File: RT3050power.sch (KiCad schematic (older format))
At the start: 30 parts, among them J1 USB, U1 RT3050, U4 LM1117, U5 LM1117

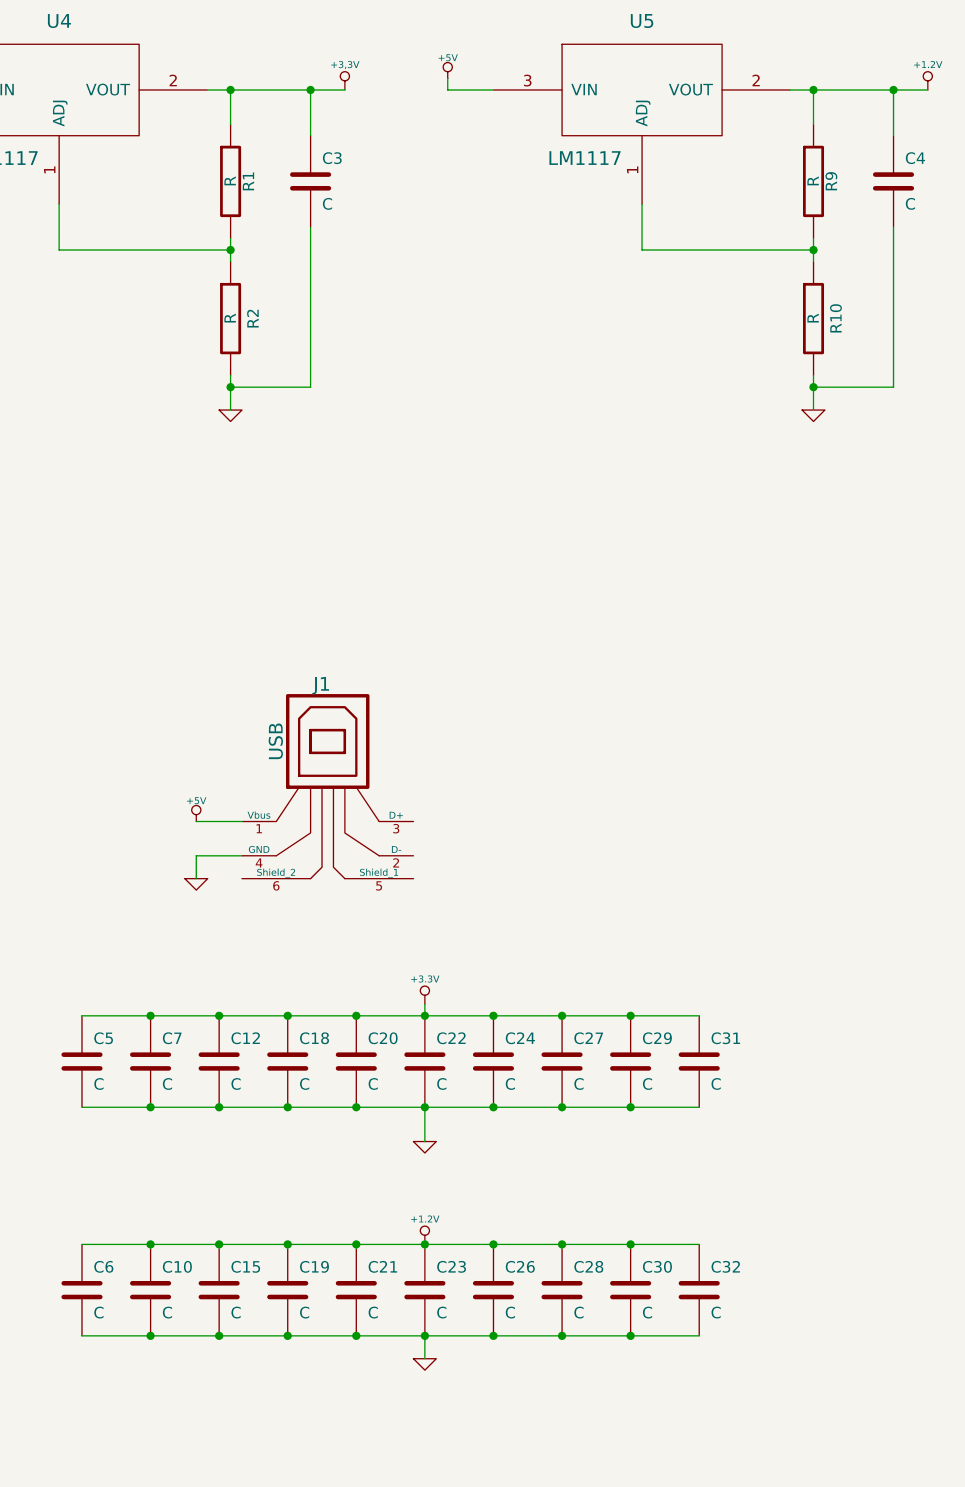
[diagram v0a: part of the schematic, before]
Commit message: updated component values
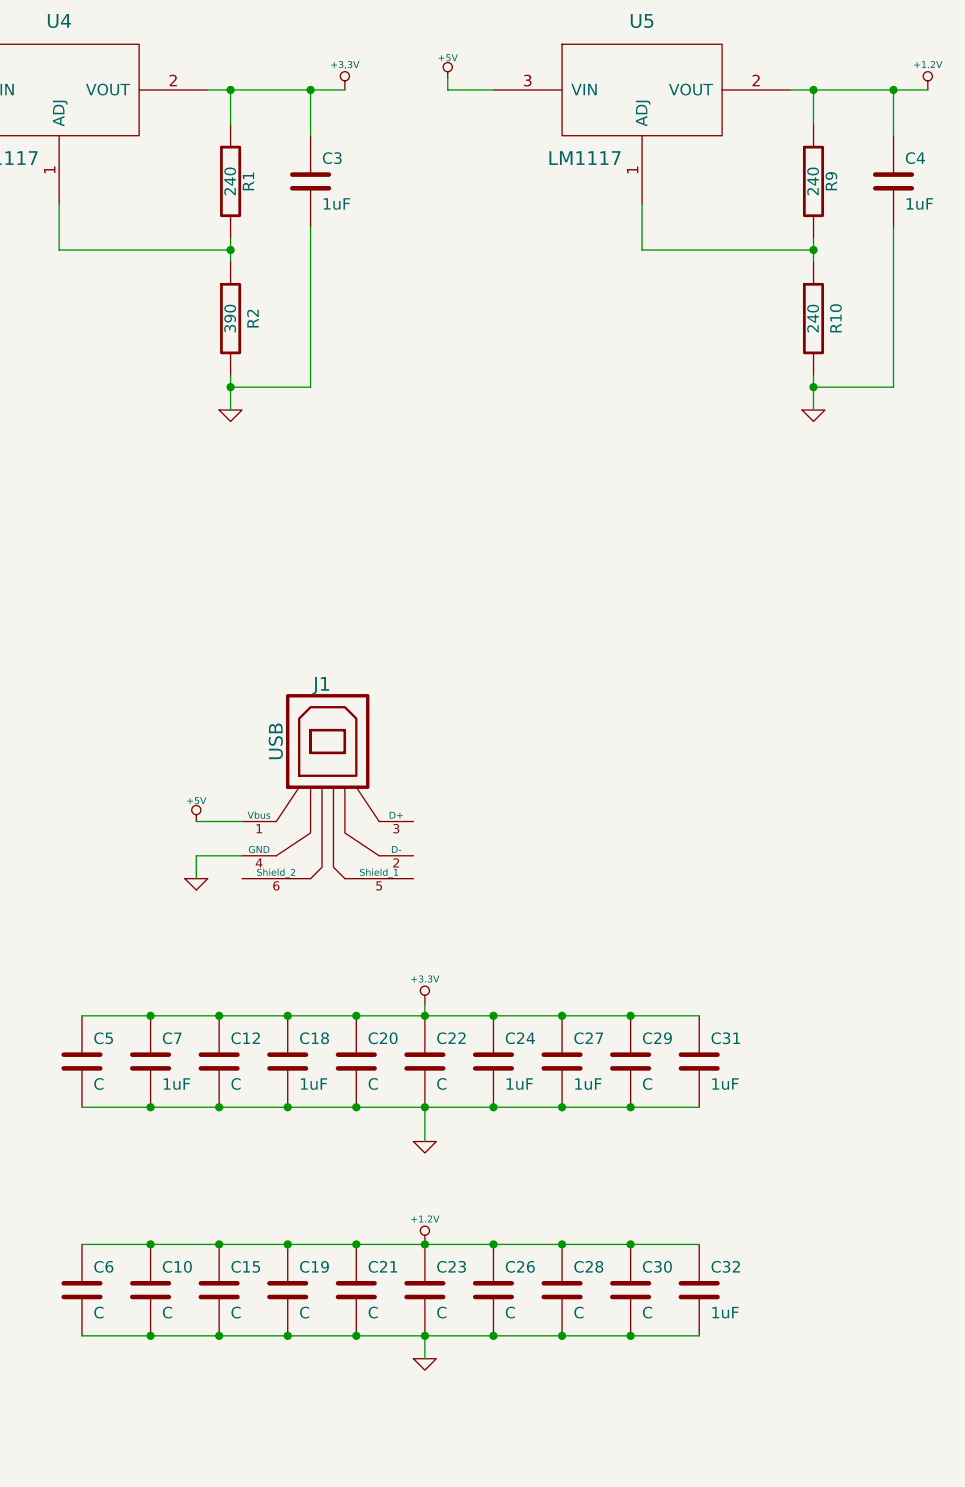
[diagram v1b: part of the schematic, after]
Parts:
- C18, C24, C27, C3, C31, C32, C4, C7: value C -> 1uF
- R1, R10, R9: value R -> 240
- R2: value R -> 390
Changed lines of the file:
@@
-EESchema Schematic File Version 2  date Tue 02 Sep 2014 05:26:51 BST
+EESchema Schematic File Version 2
 LIBS:power
 LIBS:device
@@
 LIBS:AIC809
 LIBS:rt3050-cache
-EELAYER 25  0
+EELAYER 25 0
 EELAYER END
-$Descr A4 11700 8267
+$Descr A4 11693 8268
 encoding utf-8
 Sheet 5 6
@@
 P 9750 6300
 F 0 "C32" H 9800 6400 50  0000 L CNN
-F 1 "C" H 9800 6200 50  0000 L CNN
+F 1 "1uF" H 9800 6200 50  0000 L CNN
+F 2 "" H 9750 6300 60  0001 C CNN
+F 3 "" H 9750 6300 60  0001 C CNN
 	1    9750 6300
 	1    0    0    -1
@@
 F 0 "C30" H 9500 6400 50  0000 L CNN
 F 1 "C" H 9500 6200 50  0000 L CNN
+F 2 "" H 9450 6300 60  0001 C CNN
+F 3 "" H 9450 6300 60  0001 C CNN
 	1    9450 6300
 	1    0    0    -1
@@
 F 0 "C28" H 9200 6400 50  0000 L CNN
 F 1 "C" H 9200 6200 50  0000 L CNN
+F 2 "" H 9150 6300 60  0001 C CNN
+F 3 "" H 9150 6300 60  0001 C CNN
 	1    9150 6300
 	1    0    0    -1
@@
 F 0 "C26" H 8900 6400 50  0000 L CNN
 F 1 "C" H 8900 6200 50  0000 L CNN
+F 2 "" H 8850 6300 60  0001 C CNN
+F 3 "" H 8850 6300 60  0001 C CNN
 	1    8850 6300
 	1    0    0    -1
@@
 F 0 "C23" H 8600 6400 50  0000 L CNN
 F 1 "C" H 8600 6200 50  0000 L CNN
+F 2 "" H 8550 6300 60  0001 C CNN
+F 3 "" H 8550 6300 60  0001 C CNN
 	1    8550 6300
 	1    0    0    -1
@@
 F 0 "C21" H 8300 6400 50  0000 L CNN
 F 1 "C" H 8300 6200 50  0000 L CNN
+F 2 "" H 8250 6300 60  0001 C CNN
+F 3 "" H 8250 6300 60  0001 C CNN
 	1    8250 6300
 	1    0    0    -1
@@
 F 0 "C19" H 8000 6400 50  0000 L CNN
 F 1 "C" H 8000 6200 50  0000 L CNN
+F 2 "" H 7950 6300 60  0001 C CNN
+F 3 "" H 7950 6300 60  0001 C CNN
 	1    7950 6300
 	1    0    0    -1
@@
 F 0 "C15" H 7700 6400 50  0000 L CNN
 F 1 "C" H 7700 6200 50  0000 L CNN
+F 2 "" H 7650 6300 60  0001 C CNN
+F 3 "" H 7650 6300 60  0001 C CNN
 	1    7650 6300
 	1    0    0    -1
@@
 F 0 "C10" H 7400 6400 50  0000 L CNN
 F 1 "C" H 7400 6200 50  0000 L CNN
+F 2 "" H 7350 6300 60  0001 C CNN
+F 3 "" H 7350 6300 60  0001 C CNN
 	1    7350 6300
 	1    0    0    -1
@@
 F 0 "C6" H 7100 6400 50  0000 L CNN
 F 1 "C" H 7100 6200 50  0000 L CNN
+F 2 "" H 7050 6300 60  0001 C CNN
+F 3 "" H 7050 6300 60  0001 C CNN
 	1    7050 6300
 	1    0    0    -1
@@
 P 9750 5300
 F 0 "C31" H 9800 5400 50  0000 L CNN
-F 1 "C" H 9800 5200 50  0000 L CNN
+F 1 "1uF" H 9800 5200 50  0000 L CNN
+F 2 "" H 9750 5300 60  0001 C CNN
+F 3 "" H 9750 5300 60  0001 C CNN
 	1    9750 5300
 	1    0    0    -1
@@
 F 0 "C29" H 9500 5400 50  0000 L CNN
 F 1 "C" H 9500 5200 50  0000 L CNN
+F 2 "" H 9450 5300 60  0001 C CNN
+F 3 "" H 9450 5300 60  0001 C CNN
 	1    9450 5300
 	1    0    0    -1
@@
 P 9150 5300
 F 0 "C27" H 9200 5400 50  0000 L CNN
-F 1 "C" H 9200 5200 50  0000 L CNN
+F 1 "1uF" H 9200 5200 50  0000 L CNN
+F 2 "" H 9150 5300 60  0001 C CNN
+F 3 "" H 9150 5300 60  0001 C CNN
 	1    9150 5300
 	1    0    0    -1
@@
 P 8850 5300
 F 0 "C24" H 8900 5400 50  0000 L CNN
-F 1 "C" H 8900 5200 50  0000 L CNN
+F 1 "1uF" H 8900 5200 50  0000 L CNN
+F 2 "" H 8850 5300 60  0001 C CNN
+F 3 "" H 8850 5300 60  0001 C CNN
 	1    8850 5300
 	1    0    0    -1
@@
 F 0 "C22" H 8600 5400 50  0000 L CNN
 F 1 "C" H 8600 5200 50  0000 L CNN
+F 2 "" H 8550 5300 60  0001 C CNN
+F 3 "" H 8550 5300 60  0001 C CNN
 	1    8550 5300
 	1    0    0    -1
@@
 F 0 "C20" H 8300 5400 50  0000 L CNN
 F 1 "C" H 8300 5200 50  0000 L CNN
+F 2 "" H 8250 5300 60  0001 C CNN
+F 3 "" H 8250 5300 60  0001 C CNN
 	1    8250 5300
 	1    0    0    -1
@@
 P 7950 5300
 F 0 "C18" H 8000 5400 50  0000 L CNN
-F 1 "C" H 8000 5200 50  0000 L CNN
+F 1 "1uF" H 8000 5200 50  0000 L CNN
+F 2 "" H 7950 5300 60  0001 C CNN
+F 3 "" H 7950 5300 60  0001 C CNN
 	1    7950 5300
 	1    0    0    -1
@@
 F 0 "C12" H 7700 5400 50  0000 L CNN
 F 1 "C" H 7700 5200 50  0000 L CNN
+F 2 "" H 7650 5300 60  0001 C CNN
+F 3 "" H 7650 5300 60  0001 C CNN
 	1    7650 5300
 	1    0    0    -1
@@
 P 7350 5300
 F 0 "C7" H 7400 5400 50  0000 L CNN
-F 1 "C" H 7400 5200 50  0000 L CNN
+F 1 "1uF" H 7400 5200 50  0000 L CNN
+F 2 "" H 7350 5300 60  0001 C CNN
+F 3 "" H 7350 5300 60  0001 C CNN
 	1    7350 5300
 	1    0    0    -1
@@
 F 0 "C5" H 7100 5400 50  0000 L CNN
 F 1 "C" H 7100 5200 50  0000 L CNN
+F 2 "" H 7050 5300 60  0001 C CNN
+F 3 "" H 7050 5300 60  0001 C CNN
 	1    7050 5300
 	1    0    0    -1
@@
 F 0 "#PWR027" H 8550 6600 30  0001 C CNN
 F 1 "GND" H 8550 6530 30  0001 C CNN
+F 2 "" H 8550 6600 60  0001 C CNN
+F 3 "" H 8550 6600 60  0001 C CNN
 	1    8550 6600
 	1    0    0    -1
@@
 F 0 "#PWR028" H 8550 6240 20  0001 C CNN
 F 1 "+1.2V" H 8550 6210 30  0000 C CNN
+F 2 "" H 8550 6100 60  0001 C CNN
+F 3 "" H 8550 6100 60  0001 C CNN
 	1    8550 6100
 	1    0    0    -1
@@
 F 0 "#PWR029" H 8550 5650 30  0001 C CNN
 F 1 "GND" H 8550 5580 30  0001 C CNN
+F 2 "" H 8550 5650 60  0001 C CNN
+F 3 "" H 8550 5650 60  0001 C CNN
 	1    8550 5650
 	1    0    0    -1
@@
 F 0 "#PWR030" H 8550 5010 30  0001 C CNN
 F 1 "+3.3V" H 8550 5160 30  0000 C CNN
+F 2 "" H 8550 5050 60  0001 C CNN
+F 3 "" H 8550 5050 60  0001 C CNN
 	1    8550 5050
 	1    0    0    -1
@@
 F 0 "#PWR031" H 5300 4290 20  0001 C CNN
 F 1 "+1.2V" H 5300 4260 30  0000 C CNN
+F 2 "" H 5300 4150 60  0001 C CNN
+F 3 "" H 5300 4150 60  0001 C CNN
 	1    5300 4150
 	1    0    0    -1
@@
 F 0 "#PWR032" H 5150 1090 20  0001 C CNN
 F 1 "+1.2V" H 5150 1060 30  0000 C CNN
+F 2 "" H 5150 950 60  0001 C CNN
+F 3 "" H 5150 950 60  0001 C CNN
 	1    5150 950
 	1    0    0    -1
@@
 F 0 "#PWR033" H 10750 1190 20  0001 C CNN
 F 1 "+1.2V" H 10750 1160 30  0000 C CNN
+F 2 "" H 10750 1050 60  0001 C CNN
+F 3 "" H 10750 1050 60  0001 C CNN
 	1    10750 1050
 	1    0    0    -1
@@
 F 0 "U4" H 6950 2050 60  0000 C CNN
 F 1 "LM1117" H 6700 1450 60  0000 C CNN
+F 2 "" H 6950 1400 60  0001 C CNN
+F 3 "" H 6950 1400 60  0001 C CNN
 	1    6950 1400
 	1    0    0    -1
@@
 F 0 "#PWR034" H 5100 8410 30  0001 C CNN
 F 1 "+3,3V" H 5100 8560 30  0000 C CNN
+F 2 "" H 5100 8450 60  0001 C CNN
+F 3 "" H 5100 8450 60  0001 C CNN
 	1    5100 8450
 	1    0    0    -1
@@
 P 10600 1450
 F 0 "C4" H 10650 1550 50  0000 L CNN
-F 1 "C" H 10650 1350 50  0000 L CNN
+F 1 "1uF" H 10650 1350 50  0000 L CNN
+F 2 "" H 10600 1450 60  0001 C CNN
+F 3 "" H 10600 1450 60  0001 C CNN
 	1    10600 1450
 	1    0    0    -1
@@
 P 8050 1450
 F 0 "C3" H 8100 1550 50  0000 L CNN
-F 1 "C" H 8100 1350 50  0000 L CNN
+F 1 "1uF" H 8100 1350 50  0000 L CNN
+F 2 "" H 8050 1450 60  0001 C CNN
+F 3 "" H 8050 1450 60  0001 C CNN
 	1    8050 1450
 	1    0    0    -1
@@
 F 0 "#PWR035" H 8200 1010 30  0001 C CNN
 F 1 "+3,3V" H 8200 1160 30  0000 C CNN
+F 2 "" H 8200 1050 60  0001 C CNN
+F 3 "" H 8200 1050 60  0001 C CNN
 	1    8200 1050
 	1    0    0    -1
@@
 F 0 "#PWR036" H 5450 2910 30  0001 C CNN
 F 1 "+3,3V" H 5450 3060 30  0000 C CNN
+F 2 "" H 5450 2950 60  0001 C CNN
+F 3 "" H 5450 2950 60  0001 C CNN
 	1    5450 2950
 	1    0    0    -1
@@
 P 10250 2050
 F 0 "R10" V 10350 2050 50  0000 C CNN
-F 1 "R" V 10250 2050 50  0000 C CNN
+F 1 "240" V 10250 2050 50  0000 C CNN
+F 2 "" H 10250 2050 60  0001 C CNN
+F 3 "" H 10250 2050 60  0001 C CNN
 	1    10250 2050
 	1    0    0    -1
@@
 P 10250 1450
 F 0 "R9" V 10330 1450 50  0000 C CNN
-F 1 "R" V 10250 1450 50  0000 C CNN
+F 1 "240" V 10250 1450 50  0000 C CNN
+F 2 "" H 10250 1450 60  0001 C CNN
+F 3 "" H 10250 1450 60  0001 C CNN
 	1    10250 1450
 	1    0    0    -1
@@
 F 0 "U5" H 9500 2050 60  0000 C CNN
 F 1 "LM1117" H 9250 1450 60  0000 C CNN
+F 2 "" H 9500 1400 60  0001 C CNN
+F 3 "" H 9500 1400 60  0001 C CNN
 	1    9500 1400
 	1    0    0    -1
@@
 F 0 "#PWR037" H 8650 1090 20  0001 C CNN
 F 1 "+5V" H 8650 1090 30  0000 C CNN
+F 2 "" H 8650 1000 60  0001 C CNN
+F 3 "" H 8650 1000 60  0001 C CNN
 	1    8650 1000
 	1    0    0    -1
@@
 F 0 "#PWR038" H 10250 2450 30  0001 C CNN
 F 1 "GND" H 10250 2380 30  0001 C CNN
+F 2 "" H 10250 2450 60  0001 C CNN
+F 3 "" H 10250 2450 60  0001 C CNN
 	1    10250 2450
 	1    0    0    -1
@@
 F 0 "#PWR039" H 7700 2450 30  0001 C CNN
 F 1 "GND" H 7700 2380 30  0001 C CNN
+F 2 "" H 7700 2450 60  0001 C CNN
+F 3 "" H 7700 2450 60  0001 C CNN
 	1    7700 2450
 	1    0    0    -1
@@
 F 0 "#PWR040" H 7550 4340 20  0001 C CNN
 F 1 "+5V" H 7550 4340 30  0000 C CNN
+F 2 "" H 7550 4250 60  0001 C CNN
+F 3 "" H 7550 4250 60  0001 C CNN
 	1    7550 4250
 	1    0    0    -1
@@
 F 0 "#PWR041" H 6100 1090 20  0001 C CNN
 F 1 "+5V" H 6100 1090 30  0000 C CNN
+F 2 "" H 6100 1000 60  0001 C CNN
+F 3 "" H 6100 1000 60  0001 C CNN
 	1    6100 1000
 	1    0    0    -1
@@
 F 0 "#PWR042" H 700 850 30  0001 C CNN
 F 1 "GND" H 700 780 30  0001 C CNN
+F 2 "" H 700 850 60  0001 C CNN
+F 3 "" H 700 850 60  0001 C CNN
 	1    700  850
 	1    0    0    -1
@@
 P 7700 1450
 F 0 "R1" V 7780 1450 50  0000 C CNN
-F 1 "R" V 7700 1450 50  0000 C CNN
+F 1 "240" V 7700 1450 50  0000 C CNN
+F 2 "" H 7700 1450 60  0001 C CNN
+F 3 "" H 7700 1450 60  0001 C CNN
 	1    7700 1450
 	1    0    0    -1
@@
 P 7700 2050
 F 0 "R2" V 7800 2050 50  0000 C CNN
-F 1 "R" V 7700 2050 50  0000 C CNN
+F 1 "390" V 7700 2050 50  0000 C CNN
+F 2 "" H 7700 2050 60  0001 C CNN
+F 3 "" H 7700 2050 60  0001 C CNN
 	1    7700 2050
 	1    0    0    -1
@@
 F 0 "J1" H 8100 4450 60  0000 C CNN
 F 1 "USB" V 7900 4200 60  0000 C CNN
+F 2 "" H 8150 4050 60  0001 C CNN
+F 3 "" H 8150 4050 60  0001 C CNN
 	1    8150 4050
 	1    0    0    -1
@@
 F 0 "#PWR043" H 7550 4500 30  0001 C CNN
 F 1 "GND" H 7550 4430 30  0001 C CNN
+F 2 "" H 7550 4500 60  0001 C CNN
+F 3 "" H 7550 4500 60  0001 C CNN
 	1    7550 4500
 	1    0    0    -1
@@
 F 0 "U1" H 3000 -1450 60  0000 C CNN
 F 1 "RT3050" H 2900 7900 60  0000 C CNN
+F 2 "" H 3000 4000 60  0001 C CNN
+F 3 "" H 3000 4000 60  0001 C CNN
 	3    3000 4000
 	1    0    0    -1
